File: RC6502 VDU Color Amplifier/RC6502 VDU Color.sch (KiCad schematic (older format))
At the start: 22 parts, among them J1 Video_IN, J2 Video_OUT, J3 VIDEO, J4 OSC_EN, Q1 2N3906, Q2 2N3904, U1 MC1372, Y1 3.579545

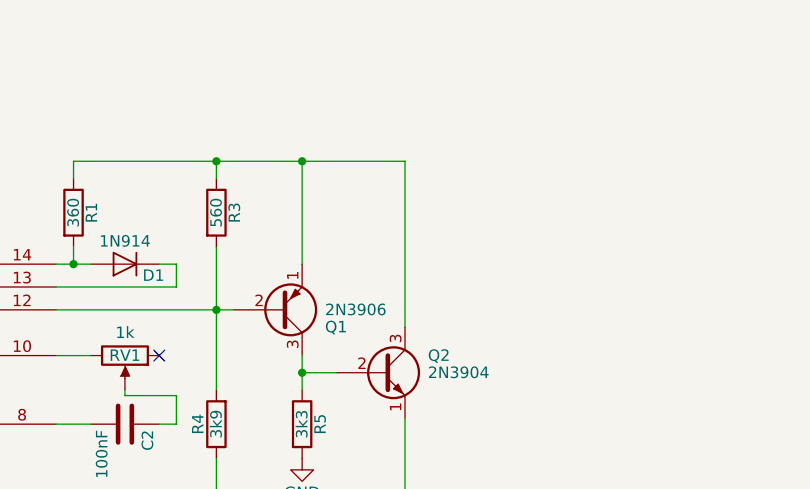
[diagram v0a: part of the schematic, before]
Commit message: Forgot to actually power amplifier circuit :-(
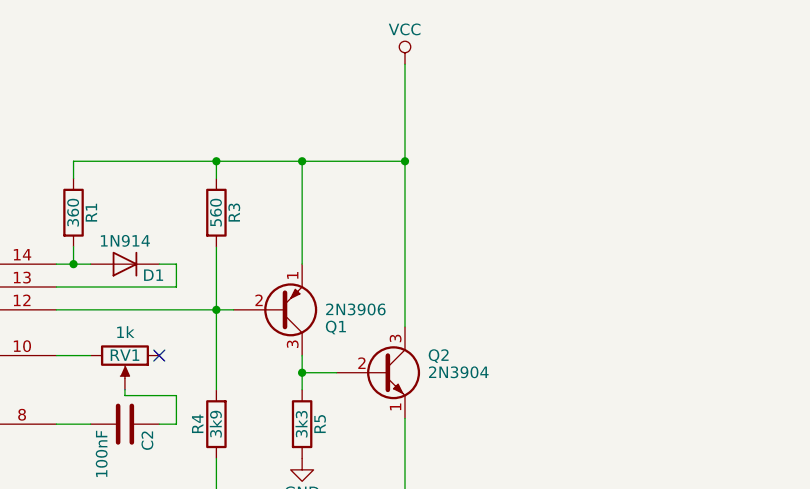
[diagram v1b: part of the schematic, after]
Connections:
- net VCC: now also Q1.1 (E), Q2.3 (C), R1.1, R3.1
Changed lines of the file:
@@
 LIBS:contrib
 LIBS:valves
-LIBS:rc6502_backplane
-LIBS:mounting
-LIBS:oscillator
-LIBS:mc6847
-LIBS:rca_plug
-LIBS:vdu_port
 LIBS:RC6502 VDU Color-cache
 EELAYER 25 0
@@
 Connection ~ 6575 2275
 Wire Wire Line
-	7025 1350 7025 2075
+	7025 925  7025 2075
 Connection ~ 6575 1350
 $Comp
@@
 NoConn ~ 1750 4975
 NoConn ~ 1750 1900
+$Comp
+L VCC #PWR?
+U 1 1 5C772014
+P 7025 925
+F 0 "#PWR?" H 7025 775 50  0001 C CNN
+F 1 "VCC" H 7025 1075 50  0000 C CNN
+F 2 "" H 7025 925 50  0001 C CNN
+F 3 "" H 7025 925 50  0001 C CNN
+	1    7025 925
+	1    0    0    -1
+$EndComp
+Connection ~ 7025 1350
 $EndSCHEMATC
